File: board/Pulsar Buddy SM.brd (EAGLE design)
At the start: 144.8 x 53.3 mm, 75 parts, among them IC1 UA78M33, IC2 ATSAMD21G18_QFN, IC3 2MB Flash, J2 MF-CON-MICROUSB-RIGHT, J3 MF-CON-2.54mm-01x12, J4 MF-CON-2.54mm-01x16, SW1 PEC11R-4220F-S0024, U1 MF-DSC-SOT233-MMBT3904, U2 MF-DSC-SOT233-MMBT3904, U3 MF-DSC-SOT233-MMBT3904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

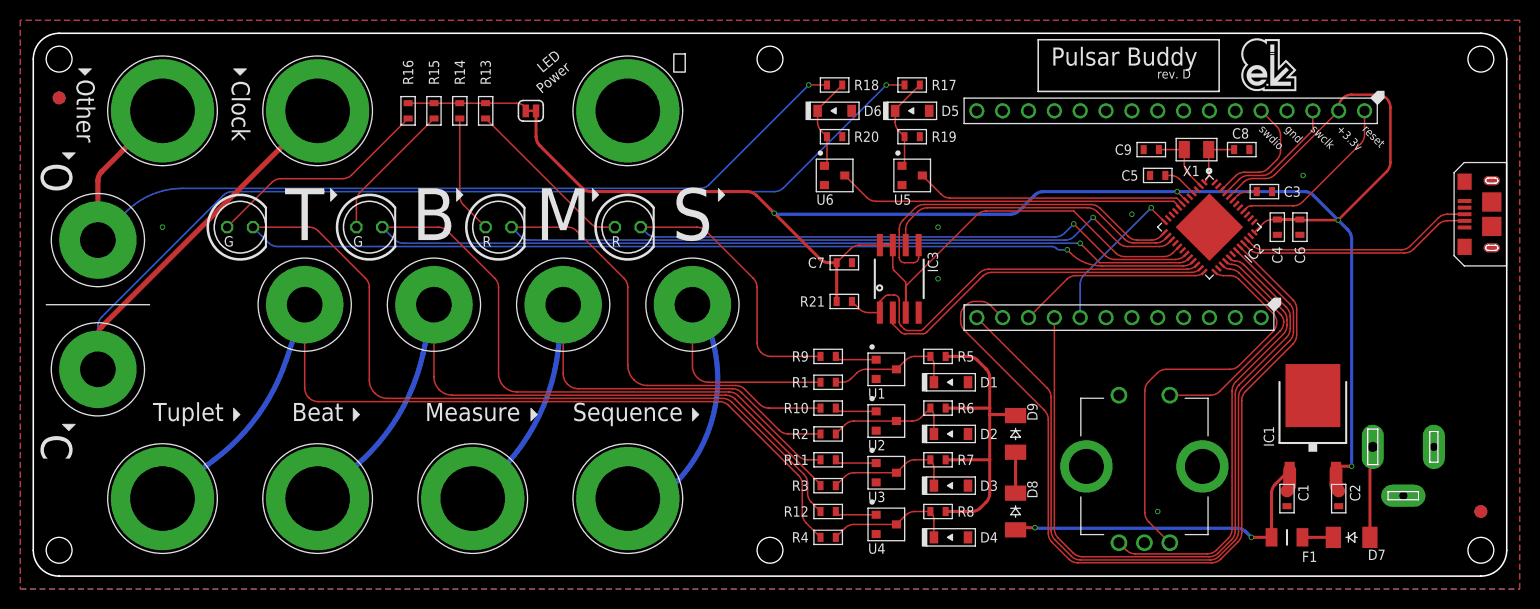
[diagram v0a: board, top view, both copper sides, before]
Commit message: rev. E board (SMT)
- smaller holes for screw posts
- minor aesthetic trace layout changes
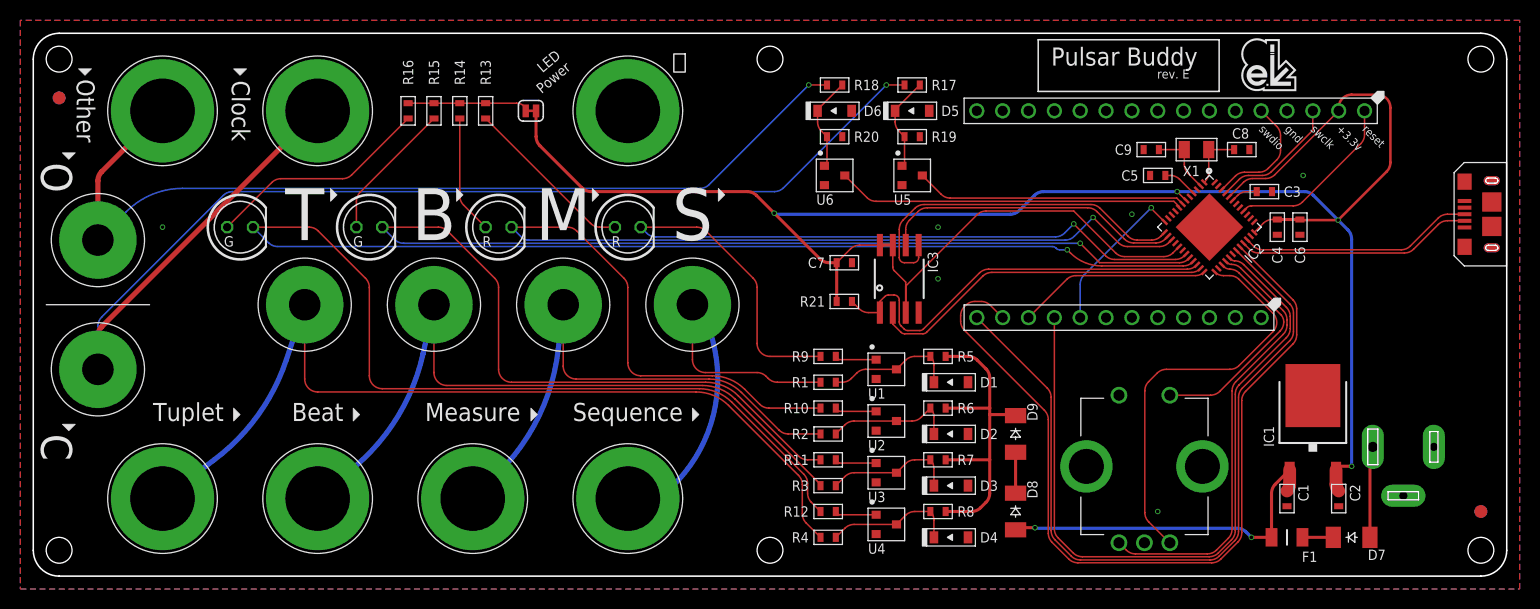
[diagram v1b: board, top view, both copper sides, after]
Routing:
- net N$39: track 91.3 -> 90.5 mm
- net N$38: track 56.0 -> 55.2 mm
- net SCK: track 138.5 -> 137.9 mm
- net N$40: track 72.4 -> 71.8 mm
- net MISO: track 167.7 -> 167.0 mm
- net D1: track 110.0 -> 109.4 mm
- net N$37: track 42.7 -> 42.1 mm
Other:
- board text added: "rev. E"
- board text removed: "rev. D"
